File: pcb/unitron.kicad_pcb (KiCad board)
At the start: 2 copper layers, 80.3 x 155.6 mm, 83 parts, among them J1 Conn_01x10_Male, J2 Conn_01x10_Female, J3 Conn_01x10_Male, J4 Conn_01x10_Female, Q1 FDN340P, Q2 BSS123, SW1 SW_SPST, U1 MCP73831-2-OT, U2 LTC-4727JS, U3 LTC-4727JS, U4 AS1115-BSST, U5 QT_Py, U7 LTC-4727JR, U8 LTC-4727JR, U9 AS1115-BSST

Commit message: pcb v1.9
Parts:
- removed the R10 at (89.4, 68.6)
- removed the R16 at (91.4, 68.6)
- removed the R17 at (87.4, 68.6)
- removed the R18 at (85.4, 68.6)
- removed R20: 10KΩ, Resistor_SMD:R_0805_2012Metric
- added R7: 10KΩ, Resistor_SMD:R_0805_2012Metric, B.Cu at (118.0, 68.0)
- added R8: 10KΩ, Resistor_SMD:R_0805_2012Metric, B.Cu at (121.0, 66.0)
- D1: renamed from D5; value SK9822 -> WS2812B; footprint asl_footprints:LED_SK9822_5050 -> LED_SMD:LED_WS2812B_PLCC4_5.0x5.0mm_P3.2mm
- D10: renamed from D6; value SK9822 -> WS2812B; footprint asl_footprints:LED_SK9822_5050 -> LED_SMD:LED_WS2812B_PLCC4_5.0x5.0mm_P3.2mm
- D2: renamed from D10; value SK9822 -> WS2812B; footprint asl_footprints:LED_SK9822_5050 -> LED_SMD:LED_WS2812B_PLCC4_5.0x5.0mm_P3.2mm
- D3: renamed from D4; value SK9822 -> WS2812B; footprint asl_footprints:LED_SK9822_5050 -> LED_SMD:LED_WS2812B_PLCC4_5.0x5.0mm_P3.2mm
- D4: renamed from D9; value SK9822 -> WS2812B; footprint asl_footprints:LED_SK9822_5050 -> LED_SMD:LED_WS2812B_PLCC4_5.0x5.0mm_P3.2mm
- D5: renamed from D3; value SK9822 -> WS2812B; footprint asl_footprints:LED_SK9822_5050 -> LED_SMD:LED_WS2812B_PLCC4_5.0x5.0mm_P3.2mm
- D6: renamed from D8; value SK9822 -> WS2812B; footprint asl_footprints:LED_SK9822_5050 -> LED_SMD:LED_WS2812B_PLCC4_5.0x5.0mm_P3.2mm
- D7: renamed from D2; value SK9822 -> WS2812B; footprint asl_footprints:LED_SK9822_5050 -> LED_SMD:LED_WS2812B_PLCC4_5.0x5.0mm_P3.2mm
- D8: renamed from D7; value SK9822 -> WS2812B; footprint asl_footprints:LED_SK9822_5050 -> LED_SMD:LED_WS2812B_PLCC4_5.0x5.0mm_P3.2mm
- D9: renamed from D1; value SK9822 -> WS2812B; footprint asl_footprints:LED_SK9822_5050 -> LED_SMD:LED_WS2812B_PLCC4_5.0x5.0mm_P3.2mm
- J1, J3: footprint Connector_PinSocket_2.54mm:PinSocket_1x10_P2.54mm_Vertical_SMD_Pin1Right -> Connector_PinSocket_2.54mm:PinSocket_1x08_P2.54mm_Vertical_SMD_Pin1Right
- J2, J4: footprint Connector_PinHeader_2.54mm:PinHeader_1x10_P2.54mm_Vertical -> Connector_PinHeader_2.54mm:PinHeader_1x08_P2.54mm_Vertical
- R11: renamed from R21; moved to B.Cu
- moved U5 48.0 mm to (126.0, 67.2), turned to 90 degrees
- moved R15 46.8 mm to (130.0, 67.0), turned to 90 degrees
- moved D13 43.7 mm to (141.0, 111.5), turned to 90 degrees
- moved R11 3.10 mm to (140.0, 68.0), turned to -90 degrees
- moved D12 2.20 mm to (137.0, 68.0), turned to -90 degrees
- moved J1 1.95 mm to (66.8, 41.3)
- moved J3 1.95 mm to (141.4, 41.3)
- moved R16 0.57 mm to (112.4, 33.8)
- moved R17 0.57 mm to (106.7, 34.4)
- moved R18 0.57 mm to (110.1, 32.7)
- moved R4 0.57 mm to (112.4, 46.6)
- moved R5 0.57 mm to (106.8, 47.1)
- moved R6 0.57 mm to (110.1, 45.5)
- moved U1 0.57 mm to (84.1, 42.4)
- moved U2 0.57 mm to (124.2, 42.4)
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- renumbered R7 to R10, R8 to R12, R15 to R13, R11 to R14, R19 to R15, R12 to R16, R13 to R17, R14 to R18, U2 to U1, U3 to U2, U4 to U3, U5 to U4, U1 to U5, U7 to U6, U8 to U7, U9 to U8
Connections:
- net /SCK renamed /neo_mcu
- D1 pad 1: /SDI -> /VIN_daughter
- D1 pad 2: /CKI -> Net-(D1-Pad2)
- D1 pad 4: /VIN_daughter -> /neopixel
- D10 pad 1: Net-(D1-Pad6) -> /VIN_daughter
- D10 pad 2: Net-(D1-Pad5) -> unconnected-(D10-Pad2)
- D10 pad 4: /VIN_daughter -> Net-(D10-Pad4)
- D2 pad 1: Net-(D10-Pad1) -> /VIN_daughter
- D2 pad 2: Net-(D10-Pad2) -> Net-(D2-Pad2)
- D2 pad 4: /VIN_daughter -> Net-(D1-Pad2)
- D3 pad 1: Net-(D10-Pad6) -> /VIN_daughter
- D3 pad 2: Net-(D10-Pad5) -> Net-(D3-Pad2)
- D3 pad 4: /VIN_daughter -> Net-(D2-Pad2)
- D4 pad 1: Net-(D4-Pad6) -> /VIN_daughter
- D4 pad 2: Net-(D4-Pad5) -> Net-(D4-Pad2)
- D4 pad 4: /VIN_daughter -> Net-(D3-Pad2)
- D5 pad 1: Net-(D3-Pad1) -> /VIN_daughter
- D5 pad 2: Net-(D3-Pad2) -> Net-(D5-Pad2)
- D5 pad 4: /VIN_daughter -> Net-(D4-Pad2)
- D6 pad 1: Net-(D3-Pad6) -> /VIN_daughter
- D6 pad 2: Net-(D3-Pad5) -> Net-(D6-Pad2)
- D6 pad 4: /VIN_daughter -> Net-(D5-Pad2)
- D7 pad 1: Net-(D2-Pad1) -> /VIN_daughter
- D7 pad 2: Net-(D2-Pad2) -> Net-(D7-Pad2)
- D7 pad 4: /VIN_daughter -> Net-(D6-Pad2)
- D8 pad 1: Net-(D2-Pad6) -> /VIN_daughter
- D8 pad 2: Net-(D2-Pad5) -> Net-(D8-Pad2)
- D8 pad 4: /VIN_daughter -> Net-(D7-Pad2)
- D9 pad 1: Net-(D1-Pad1) -> /VIN_daughter
- D9 pad 2: Net-(D1-Pad2) -> Net-(D10-Pad4)
- D9 pad 4: /VIN_daughter -> Net-(D8-Pad2)
- J1 pad 1: unconnected-(J1-Pad1) -> /a
- J1 pad 2: /a -> /b
- J1 pad 3: /b -> /c
- J1 pad 4: /c -> /d
- J1 pad 5: /d -> /e
- J1 pad 6: /e -> /f
- J1 pad 7: /f -> /g
- J1 pad 8: /g -> /dp
- J2 pad 1: unconnected-(J2-Pad1) -> Net-(J2-Pad1)
- J3 pad 8: /CKI -> /neopixel
- J4 pad 2: /VIN -> /3VDC
- R11 pad 1: /VBATT -> Net-(D12-Pad1)
- R15 pad 1: Net-(D12-Pad1) -> GND
- S10 pad 2: Net-(J2-Pad4) -> Net-(J2-Pad3)
- S11 pad 2: Net-(J2-Pad5) -> Net-(J2-Pad4)
- S12 pad 2: Net-(J2-Pad6) -> Net-(J2-Pad5)
- S13 pad 2: Net-(J2-Pad7) -> Net-(J2-Pad6)
- S14 pad 2: Net-(J2-Pad8) -> Net-(J2-Pad7)
- S15 pad 2: Net-(J2-Pad9) -> Net-(J2-Pad8)
- S2 pad 2: Net-(J2-Pad2) -> Net-(J2-Pad1)
- S3 pad 2: Net-(J2-Pad3) -> Net-(J2-Pad2)
- S4 pad 2: Net-(J2-Pad4) -> Net-(J2-Pad3)
- S5 pad 2: Net-(J2-Pad5) -> Net-(J2-Pad4)
- S6 pad 2: Net-(J2-Pad6) -> Net-(J2-Pad5)
- S7 pad 2: Net-(J2-Pad9) -> Net-(J2-Pad8)
- S8 pad 2: Net-(J2-Pad2) -> Net-(J2-Pad1)
- S9 pad 2: Net-(J2-Pad3) -> Net-(J2-Pad2)
- U4 pad 1: unconnected-(U5-Pad1) -> Net-(R7-Pad1)
- U4 pad 11: /MOSI -> unconnected-(U4-Pad11)
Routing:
- net Net-(J2-Pad1): track 0.00 -> 121.2 mm, vias 0 -> 2
- net Net-(J2-Pad9): track 99.9 -> 0.00 mm, vias 1 -> 0
- net /VBATT: track 73.6 -> 13.6 mm, vias 1 -> 0
- net /MOSI: track 59.6 -> 0.00 mm, vias 1 -> 0
- net Net-(J2-Pad6): track 106.4 -> 60.4 mm, vias 0 -> 1
- net Net-(D13-Pad2): track 3.68 -> 45.4 mm, vias 0 -> 1
- net /3VDC: track 30.8 -> 65.3 mm
- net Net-(J2-Pad8): track 72.8 -> 102.4 mm
- net Net-(J2-Pad4): track 149.1 -> 123.1 mm, vias 3 -> 1
- net Net-(J2-Pad3): track 133.2 -> 152.9 mm, vias 2 -> 3
- net Net-(D13-Pad1): track 69.9 -> 51.6 mm, vias 1 -> 3
- net Net-(D8-Pad2): track 0.00 -> 17.2 mm
- net Net-(D4-Pad2): track 0.00 -> 16.2 mm
- net Net-(D1-Pad1): track 15.7 -> 0.00 mm
- net /CKI: track 14.8 -> 0.00 mm, vias 1 -> 0
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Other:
- board size 80.3 x 155.6 mm -> 80.3 x 155 mm
- board text added: "Dec 2021"
- board text added: "Unitron v1.9"
- board text removed: "May 2021"
- board text removed: "Unitron v1.8"

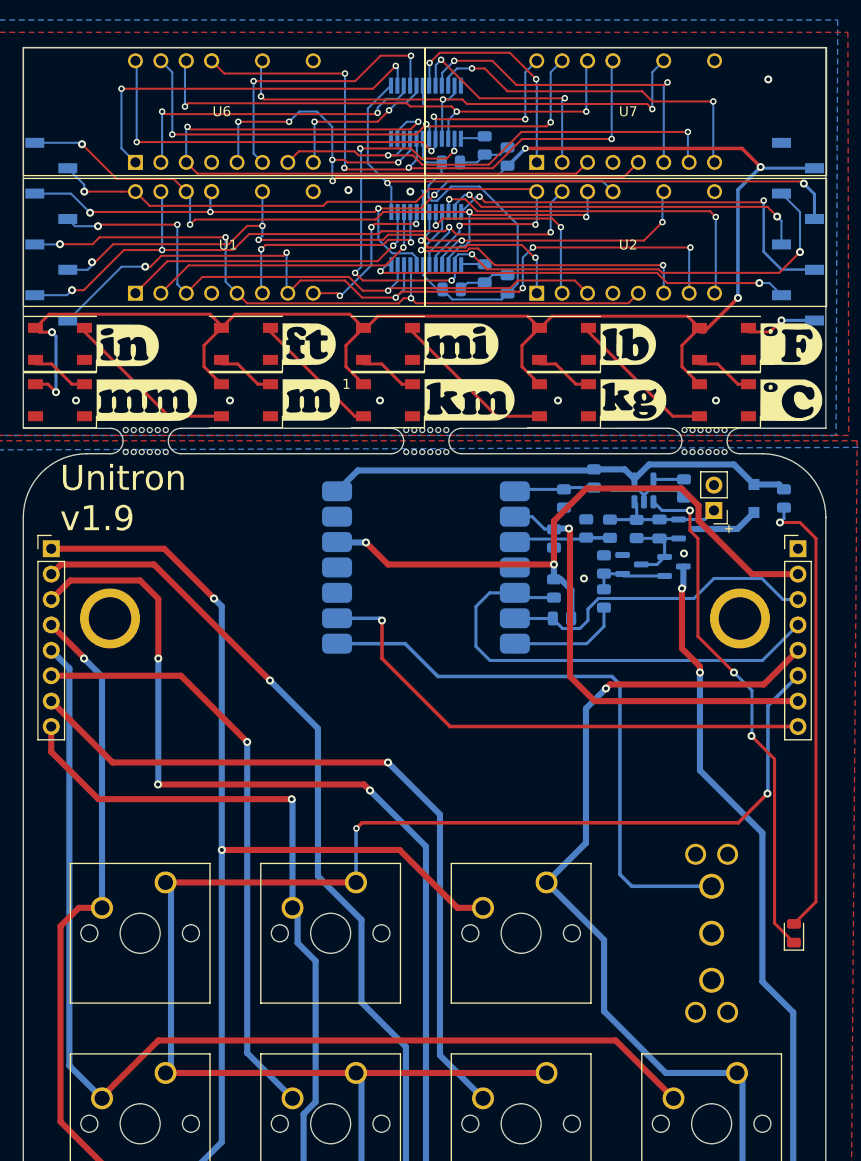
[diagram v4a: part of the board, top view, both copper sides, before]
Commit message: v1.10
shift as1115 label closer to pin 1
remove "1"  label from km neopixel
make IRQ trace and via larger.
change i2c pullups from 10k to 2k
added diodes to keyscan traces so multiple buttons can simultaneously be pressed
make cutout for different qt py
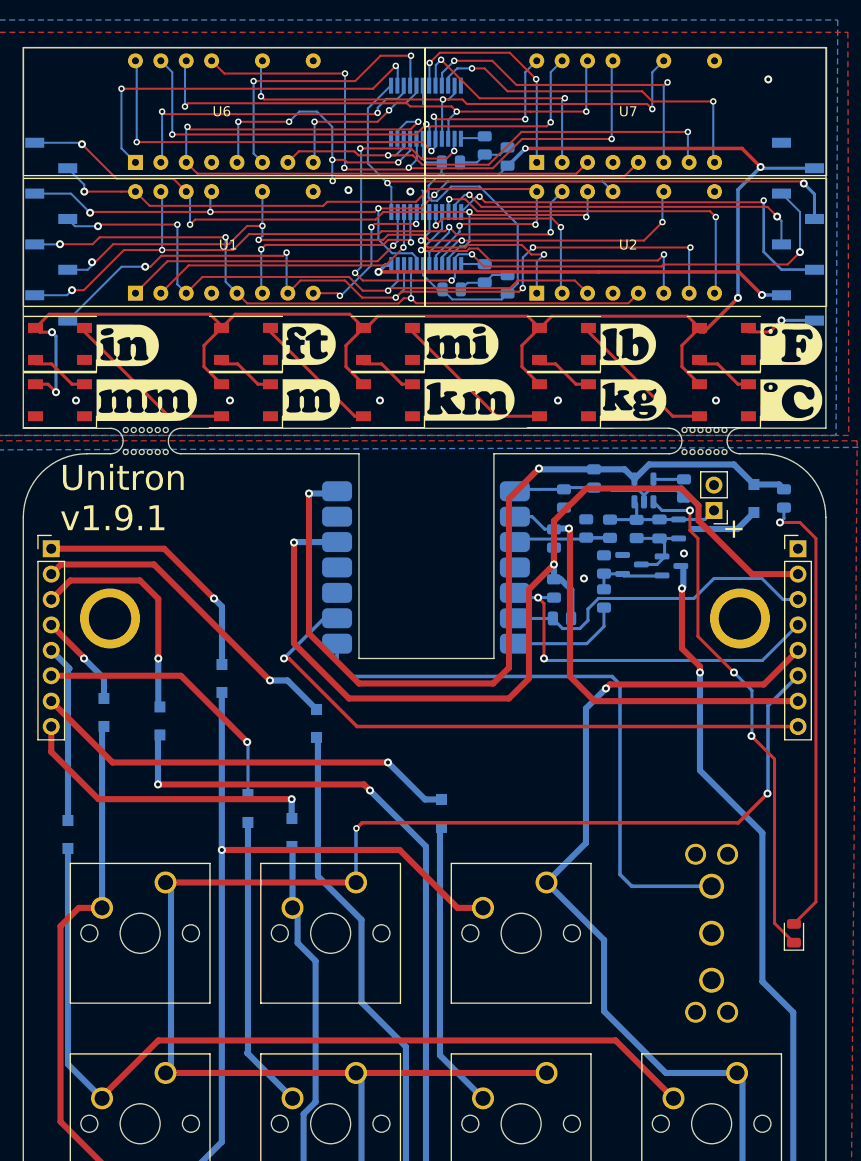
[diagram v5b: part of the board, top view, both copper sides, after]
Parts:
- removed the MB* at (104.3, 62.2)
- added D14: Diode, asl_footprints:D_SOD-123F, B.Cu at (90.8, 101.4)
- added D15: Diode, asl_footprints:D_SOD-123F, B.Cu at (83.8, 86.0)
- added D16: Diode, asl_footprints:D_SOD-123F, B.Cu at (72.0, 89.4)
- added D17: Diode, asl_footprints:D_SOD-123F, B.Cu at (68.4, 101.6)
- added D18: Diode, asl_footprints:D_SOD-123F, B.Cu at (93.3, 90.5)
- added D19: Diode, asl_footprints:D_SOD-123F, B.Cu at (105.8, 99.5)
- added D20: Diode, asl_footprints:D_SOD-123F, B.Cu at (77.6, 90.2)
- added D21: Diode, asl_footprints:D_SOD-123F, B.Cu at (86.4, 99.0)
- R13, R14: value 10KΩ -> 12KΩ
- moved D11 0.25 mm to (128.8, 74.7)
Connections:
- S10 pad 2: Net-(J2-Pad3) -> Net-(S10-Pad2)
- S11 pad 2: Net-(J2-Pad4) -> Net-(S11-Pad2)
- S12 pad 2: Net-(J2-Pad5) -> Net-(S12-Pad2)
- S13 pad 2: Net-(J2-Pad6) -> Net-(S13-Pad2)
- S14 pad 2: Net-(J2-Pad7) -> Net-(S14-Pad2)
- S15 pad 2: Net-(J2-Pad8) -> Net-(S15-Pad2)
- S2 pad 2: Net-(J2-Pad1) -> Net-(S2-Pad2)
- S3 pad 2: Net-(J2-Pad2) -> Net-(S3-Pad2)
- S4 pad 2: Net-(J2-Pad3) -> Net-(S10-Pad2)
- S5 pad 2: Net-(J2-Pad4) -> Net-(S11-Pad2)
- S6 pad 2: Net-(J2-Pad5) -> Net-(S12-Pad2)
- S7 pad 2: Net-(J2-Pad8) -> Net-(S15-Pad2)
- S8 pad 2: Net-(J2-Pad1) -> Net-(S2-Pad2)
- S9 pad 2: Net-(J2-Pad2) -> Net-(S3-Pad2)
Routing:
- net Net-(J2-Pad3): track 152.9 -> 23.1 mm, vias 3 -> 1
- net Net-(S10-Pad2): track 0.00 -> 127.1 mm, vias 0 -> 2
- net Net-(J2-Pad4): track 123.1 -> 9.54 mm
- net Net-(S11-Pad2): track 0.00 -> 110.9 mm
- net Net-(J2-Pad2): track 133.7 -> 32.9 mm, vias 2 -> 1
- net Net-(S3-Pad2): track 0.00 -> 99.0 mm, vias 0 -> 1
- net Net-(J2-Pad1): track 121.2 -> 25.3 mm, vias 2 -> 1
- net Net-(S2-Pad2): track 0.00 -> 93.1 mm, vias 0 -> 1
- net Net-(J2-Pad5): track 109.0 -> 17.8 mm
- net Net-(S12-Pad2): track 0.00 -> 88.4 mm
- net Net-(J2-Pad8): track 102.4 -> 30.6 mm
- net Net-(S15-Pad2): track 0.00 -> 69.1 mm
- net Net-(D12-Pad1): track 47.6 -> 87.5 mm, vias 0 -> 2
- net Net-(J2-Pad6): track 60.4 -> 27.6 mm
- net /3VDC: track 65.3 -> 96.2 mm
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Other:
- outline, holes or cut-outs redrawn
- board text added: "Unitron v1.9.1"
- board text removed: "Unitron v1.9"

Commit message: v 1.11
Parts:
- removed C1: 10nF, Capacitor_SMD:C_0805_2012Metric
- removed D11: BAT54C, Package_TO_SOT_SMD:SOT-23
- removed Q1: FDN340P, Package_TO_SOT_SMD:SOT-23
- removed Q2: BSS123, Package_TO_SOT_SMD:SOT-23
- added C2: 10nF, Capacitor_SMD:C_0805_2012Metric, B.Cu at (104.8, 49.5)
- added C3: 10nF, Capacitor_SMD:C_0805_2012Metric, B.Cu at (106.8, 49.5)
- added R19: 10KΩ, Resistor_SMD:R_0805_2012Metric, B.Cu at (71.5, 35.0)
- added R20: 10KΩ, Resistor_SMD:R_0805_2012Metric, B.Cu at (71.5, 40.0)
- added R21: 10KΩ, Resistor_SMD:R_0805_2012Metric, B.Cu at (71.5, 37.5)
- added R22: 10KΩ, Resistor_SMD:R_0805_2012Metric, B.Cu at (71.5, 42.5)
- added R23: 10KΩ, Resistor_SMD:R_0805_2012Metric, B.Cu at (71.5, 45.0)
- added R24: 10KΩ, Resistor_SMD:R_0805_2012Metric, B.Cu at (71.5, 47.8)
- added R25: 10KΩ, Resistor_SMD:R_0805_2012Metric, B.Cu at (71.5, 50.2)
- added TP1: TestPoint, TestPoint:TestPoint_Pad_1.0x1.0mm, B.Cu at (111.8, 42.2)
- added TP2: TestPoint, TestPoint:TestPoint_Pad_1.0x1.0mm, B.Cu at (100.8, 37.5)
- added TP3: TestPoint, TestPoint:TestPoint_Pad_1.0x1.0mm, B.Cu at (99.5, 46.0)
- R1: value 100KΩ -> 10Ω
- R13, R14: value 12KΩ -> 1KΩ
- R2: value 330Ω -> 10Ω
- R3: value 1MΩ -> 10KΩ
- moved R3 65.8 mm to (71.5, 32.5), turned to 0 degrees
- moved R2 38.9 mm to (134.7, 41.2), turned to 180 degrees
- moved R1 36.4 mm to (136.5, 36.4), turned to 180 degrees
- moved R18 3.27 mm to (110.0, 29.4)
- moved R5 3.13 mm to (109.2, 49.0), turned to -90 degrees
- moved R17 2.85 mm to (109.4, 33.4), turned to -90 degrees
- moved R4 2.81 mm to (111.0, 49.0)
- moved R16 2.59 mm to (111.8, 31.2)
- moved R13 0.90 mm to (117.8, 77.5), turned to 0 degrees
- moved R6 0.89 mm to (109.2, 45.8)
- moved R14 0.08 mm to (117.8, 80.0)
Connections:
- D12 pad 2: /VIN -> /VBATT
- J1 pad 1: /a -> Net-(J1-Pad1)
- J1 pad 2: /b -> Net-(J1-Pad2)
- J1 pad 3: /c -> Net-(J1-Pad3)
- J1 pad 4: /d -> Net-(J1-Pad4)
- J1 pad 5: /e -> Net-(J1-Pad5)
- J1 pad 6: /f -> Net-(J1-Pad6)
- J1 pad 7: /g -> Net-(J1-Pad7)
- J1 pad 8: /dp -> Net-(J1-Pad8)
- J3 pad 3: /SCL -> Net-(J3-Pad3)
- J3 pad 4: /SDA -> Net-(J3-Pad4)
- R1 pad 1: Net-(C1-Pad2) -> Net-(J3-Pad4)
- R1 pad 2: /VBATT -> /SDA
- R2 pad 1: /BTN -> Net-(J3-Pad3)
- R2 pad 2: Net-(D11-Pad1) -> /SCL
- R3 pad 1: GND -> Net-(J1-Pad1)
- R3 pad 2: Net-(D11-Pad1) -> /a
- S1 pad 1: Net-(D11-Pad3) -> /BTN
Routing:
- net Net-(D11-Pad3): track 97.0 -> 0.00 mm, vias 2 -> 0
- net /BTN: track 11.5 -> 97.9 mm
- net /VIN_daughter: track 205.6 -> 188.0 mm, vias 5 -> 6
- net /3VDC: track 96.2 -> 81.6 mm, vias 2 -> 3
- net /SCL: track 78.9 -> 65.9 mm, vias 6 -> 4
- net /SDA: track 60.4 -> 51.0 mm
- net Net-(C1-Pad2): track 8.98 -> 0.00 mm
- net Net-(J3-Pad4): track 0.00 -> 8.13 mm
- net /g: track 69.9 -> 61.9 mm
- net /mode: track 59.7 -> 51.9 mm
- net Net-(D11-Pad1): track 7.68 -> 0.00 mm
- net /VBATT: track 13.6 -> 20.5 mm, vias 0 -> 1
- net /c: track 70.8 -> 64.1 mm
- net /VIN: track 6.28 -> 0.00 mm
- net /e: track 70.2 -> 63.9 mm
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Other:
- outline, holes or cut-outs redrawn
- board text added: "Feb 2022"
- board text added: "SCL"
- board text added: "SDA"
- board text added: "Unitron v1.11"
- board text added: "v1.11"
- board text removed: "Dec 2021"
- board text removed: "Unitron v1.9.1"

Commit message: pcb v1.12
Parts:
- removed D14, D15, D16, D17, D18, D19, D20, D21: Diode, asl_footprints:D_SOD-123F
- removed the R1 at (136.5, 36.4)
- removed the R2 at (134.7, 41.2)
- added SW1: SPST_B12AP, asl_footprints:switch_toggle, F.Cu at (138.0, 111.5)
- C1: renamed from C2; value 10nF -> 1µF
- C2: renamed from C3; value 10nF -> 100nF
- R18: renamed from R13; value 1KΩ -> 2KΩ
- R19: renamed from R14; value 1KΩ -> 2KΩ
- R20: renamed from R15; value 10KΩ -> 2KΩ
- moved D12 7.13 mm to (138.0, 105.0), turned to 0 degrees
- moved SW2 5.29 mm to (127.5, 111.5)
- moved D11 4.03 mm to (133.0, 68.0)
- moved BT1 2.99 mm to (136.0, 69.5)
- renumbered D12 to D11, D13 to D12, R4 to R1, R24 to R10, R25 to R11, R7 to R12, R8 to R13, R9 to R14, R10 to R15, R11 to R16, R12 to R17, R5 to R2, R16 to R21, R17 to R22, R18 to R23, R6 to R3, R3 to R4, R19 to R5, R20 to R6, R21 to R7, R22 to R8, R23 to R9, SW1 to SW2
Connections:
- BT1 pad 1: /VBATT -> Net-(BT1-Pad1)
- J2 pad 1: Net-(D15-Pad2) -> Net-(J2-Pad1)
- J2 pad 2: Net-(D18-Pad2) -> Net-(J2-Pad2)
- J2 pad 3: Net-(D20-Pad2) -> Net-(J2-Pad3)
- J2 pad 4: Net-(D16-Pad2) -> Net-(J2-Pad4)
- J2 pad 5: Net-(D17-Pad2) -> Net-(J2-Pad5)
- J2 pad 6: Net-(D21-Pad2) -> Net-(J2-Pad6)
- J2 pad 7: Net-(D19-Pad2) -> Net-(J2-Pad7)
- J2 pad 8: Net-(D14-Pad2) -> Net-(J2-Pad8)
- J3 pad 3: Net-(J3-Pad3) -> /SCL
- J3 pad 4: Net-(J3-Pad4) -> /SDA
- S10 pad 2: Net-(D20-Pad1) -> Net-(J2-Pad3)
- S11 pad 2: Net-(D16-Pad1) -> Net-(J2-Pad4)
- S12 pad 2: Net-(D17-Pad1) -> Net-(J2-Pad5)
- S13 pad 2: Net-(D21-Pad1) -> Net-(J2-Pad6)
- S14 pad 2: Net-(D19-Pad1) -> Net-(J2-Pad7)
- S15 pad 2: Net-(D14-Pad1) -> Net-(J2-Pad8)
- S2 pad 2: Net-(D15-Pad1) -> Net-(J2-Pad1)
- S3 pad 2: Net-(D18-Pad1) -> Net-(J2-Pad2)
- S4 pad 2: Net-(D20-Pad1) -> Net-(J2-Pad3)
- S5 pad 2: Net-(D16-Pad1) -> Net-(J2-Pad4)
- S6 pad 2: Net-(D17-Pad1) -> Net-(J2-Pad5)
- S7 pad 2: Net-(D14-Pad1) -> Net-(J2-Pad8)
- S8 pad 2: Net-(D15-Pad1) -> Net-(J2-Pad1)
- S9 pad 2: Net-(D18-Pad1) -> Net-(J2-Pad2)
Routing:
- net Net-(J2-Pad3): track 0.00 -> 152.4 mm, vias 0 -> 2
- net Net-(J2-Pad2): track 0.00 -> 133.7 mm, vias 0 -> 2
- net Net-(D20-Pad1): track 127.1 -> 0.00 mm, vias 2 -> 0
- net Net-(J2-Pad4): track 0.00 -> 123.1 mm
- net Net-(J2-Pad1): track 0.00 -> 119.5 mm, vias 0 -> 1
- net Net-(D16-Pad1): track 110.9 -> 0.00 mm
- net Net-(J2-Pad5): track 0.00 -> 109.0 mm
- net Net-(J2-Pad8): track 0.00 -> 102.4 mm, vias 0 -> 1
- net Net-(D18-Pad1): track 99.0 -> 0.00 mm, vias 1 -> 0
- net Net-(D15-Pad1): track 93.1 -> 0.00 mm, vias 1 -> 0
- net Net-(D17-Pad1): track 88.4 -> 0.00 mm
- net Net-(J2-Pad7): track 0.00 -> 73.7 mm, vias 0 -> 1
- net Net-(D14-Pad1): track 69.1 -> 0.00 mm
- net Net-(J2-Pad6): track 0.00 -> 60.5 mm, vias 0 -> 1
- net Net-(BT1-Pad1): track 0.00 -> 52.6 mm
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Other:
- board text added: "Mar 2022"
- board text added: "Unitron v1.12"
- board text added: "v1.12"
- board text removed: "Feb 2022"
- board text removed: "Unitron v1.11"
- board text removed: "v1.11"

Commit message: pcb v1.13
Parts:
- removed D10, D9: WS2812B, LED_SMD:LED_WS2812B_PLCC4_5.0x5.0mm_P3.2mm
- removed the D7 at (86.2, 52.5)
- removed the D8 at (86.2, 58.1)
- removed G*** (x10): LOGO, LOGO
- removed the S6 at (135.3, 125.4)
- added C3: 10µF, Capacitor_SMD:C_0805_2012Metric, B.Cu at (130.0, 70.8)
- added SW3: RotaryEncoder_Switch, asl_footprints:encoder_PEC11R, F.Cu at (132.8, 130.5)
- added kibuzzard-6260D796: G***, kibuzzard-6260D796, F.Cu at (98.5, 58.0)
- added kibuzzard-6260D7DE: G***, kibuzzard-6260D7DE, F.Cu at (112.0, 58.0)
- added kibuzzard-6260D82F: G***, kibuzzard-6260D82F, F.Cu at (125.5, 58.0)
- added kibuzzard-6260D857: G***, kibuzzard-6260D857, F.Cu at (139.0, 58.0)
- added kibuzzard-6260D976: G***, kibuzzard-6260D976, F.Cu at (85.0, 58.0)
- added kibuzzard-6260DA5E: G***, kibuzzard-6260DA5E, F.Cu at (71.5, 58.0)
- SW1: value SPST_B12AP -> SPST
- U5: value MCP73831-2-OT -> MCP73831
- moved D6 29.5 mm to (71.5, 52.5)
- moved D4 20.3 mm to (98.5, 52.5)
- moved D5 15.4 mm to (85.0, 52.5)
- moved D2 10.2 mm to (125.5, 52.5)
- moved D3 6.03 mm to (112.0, 52.5)
- moved D1 4.97 mm to (139.0, 52.5)
- moved D8 4.72 mm to (140.5, 101.0)
- moved BT1 2.50 mm to (136.0, 67.0), turned to 0 degrees
- moved SW2 1.35 mm to (128.9, 111.5)
- moved SW1 1.27 mm to (136.7, 111.5), turned to 0 degrees
- moved U5 0.18 mm to (126.0, 67.0)
- renumbered D11 to D7, D12 to D8, S11 to S10, S12 to S11, S13 to S12, S14 to S13, S15 to S14, S7 to S6, S8 to S7, S9 to S8, S10 to S9
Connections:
- D6 pad 2: Net-(D6-Pad2) -> unconnected-(D6-Pad2)
- U4 pad 10: unconnected-(U4-Pad10) -> /encoder_b
- U4 pad 11: unconnected-(U4-Pad11) -> /encoder_a
- U4 pad 4: unconnected-(U4-Pad4) -> /encoder_btn
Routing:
- net /encoder_a: track 0.00 -> 98.7 mm, vias 0 -> 1
- net /encoder_b: track 0.00 -> 95.6 mm, vias 0 -> 1
- net /encoder_btn: track 0.00 -> 65.5 mm, vias 0 -> 3
- net Net-(J2-Pad5): track 109.0 -> 46.7 mm
- net /VIN_daughter: track 188.0 -> 142.1 mm, vias 6 -> 4
- net Net-(J2-Pad2): track 133.7 -> 159.4 mm, vias 2 -> 3
- net Net-(D8-Pad2) (its old number): track 17.2 -> 0.00 mm
- net Net-(D6-Pad2): track 12.8 -> 0.00 mm
- net /KEYA: track 167.8 -> 161.1 mm
- net Net-(D4-Pad2): track 16.2 -> 9.66 mm
- net Net-(BT1-Pad1): track 52.6 -> 46.2 mm
- net Net-(D10-Pad4): track 5.74 -> 0.00 mm
- net Net-(D7-Pad2): track 5.74 -> 0.00 mm
- net Net-(D8-Pad1): track 45.6 -> 39.9 mm
- net Net-(D8-Pad2): track 40.7 -> 35.2 mm
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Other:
- outline, holes or cut-outs redrawn
- board text added: "IRQ"
- board text added: "Lustig Labworks April 2022"
- board text added: "R4-R11"
- board text added: "Unitron v1.13"
- board text added: "v1.13"
- board text removed: "Mar 2022"
- board text removed: "Unitron v1.12"
- board text removed: "v1.12"
